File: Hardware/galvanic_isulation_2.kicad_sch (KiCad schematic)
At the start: 14 parts

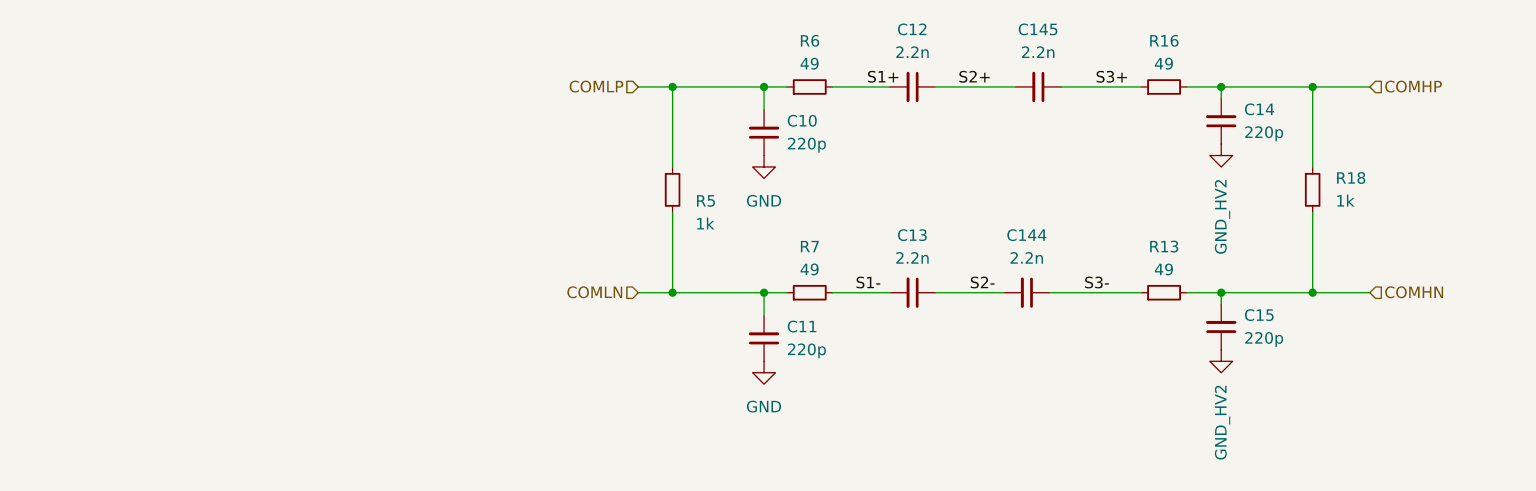
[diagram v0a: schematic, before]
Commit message: Bms plug and play, 2nd iteration with the same pinout
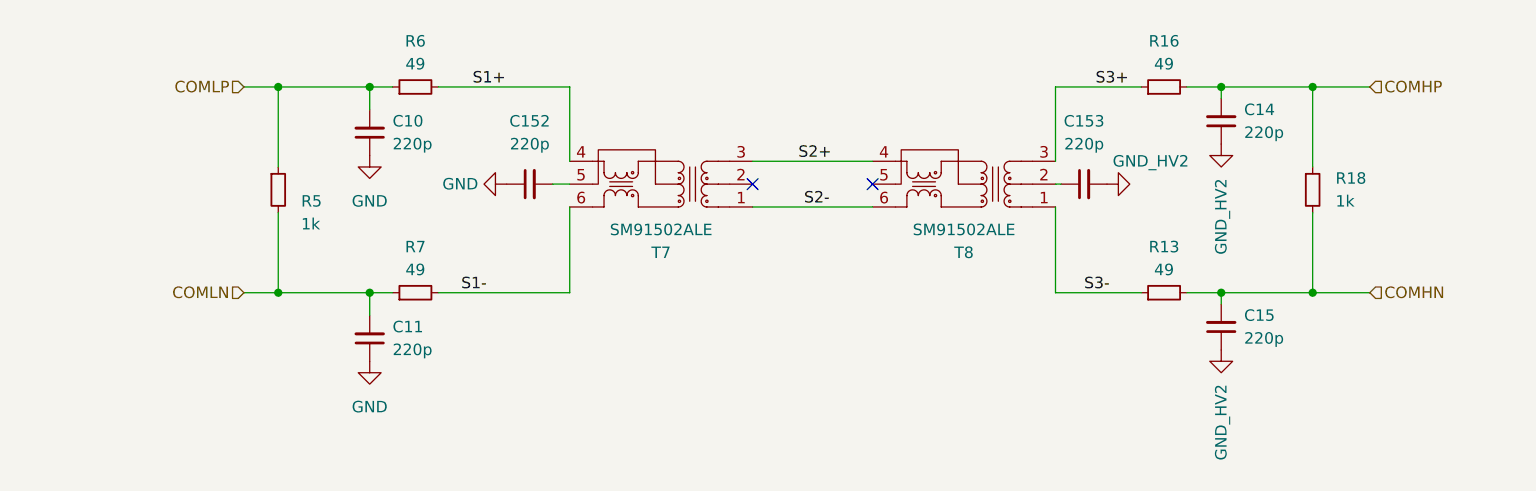
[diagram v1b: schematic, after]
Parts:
- removed C12, C13, C144, C145: 2.2n, footrpint:CAPC5728X280N, symbol Device:C_Small
- added C152, C153: 220p, Capacitor_SMD:C_0603_1608Metric_Pad1.08x0.95mm_HandSolder, symbol Device:C_Small
- added T7, T8: SM91502ALE, footrpint:SOP254P927X572-6N, symbol Samacsys:SM91502ALE
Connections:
- net GND: now also C152.1
- net GND_HV2: now also C153.2
- net S1+: now also T7.4 (SEC_1)
- net S1-: now also T7.6 (SEC_3)
- net S2+: now also T7.3 (PRI_3), T8.4 (SEC_1)
- net S2-: now also T7.1 (PRI_1), T8.6 (SEC_3)
- net S3+: now also T8.3 (PRI_3)
- net S3-: now also T8.1 (PRI_1)
- new net: C153.1, T8.2 (PRI_2)
- new net: C152.2, T7.5 (SEC_2)
- no-connect marks 0 -> 2
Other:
- moved on the sheet: C10, C11, R5, R6, R7

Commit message: New connectors jst_xh for low voltage side of bms
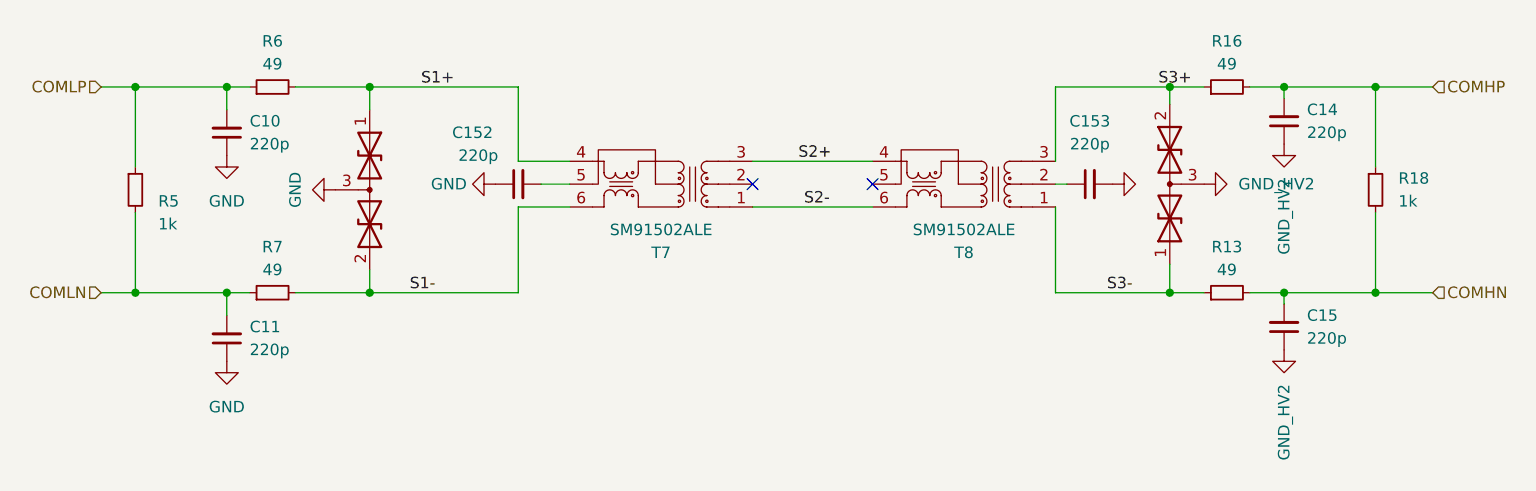
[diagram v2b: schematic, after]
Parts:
- added D40, D41: 13.3V tvs, Package_TO_SOT_SMD:SOT-23, symbol Device:D_TVS_Dual_AAC
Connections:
- net GND: now also D40.3 (common)
- net GND_HV2: now also D41.3 (common)
- net S1+: now also D40.1 (A1)
- net S1-: now also D40.2 (A2)
- net S3+: now also D41.2 (A2)
- net S3-: now also D41.1 (A1)
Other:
- title: (none) -> Battery Management System for a high power gokart battery
- moved on the sheet: C10, C11, C14, C15, C152, C153, R13, R16, R18, R5, R6, R7
